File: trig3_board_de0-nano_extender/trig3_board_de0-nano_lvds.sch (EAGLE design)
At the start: 75 parts, among them IC1 SN65LVDT388ADBT, IC2 SN65LVDT388ADBT, J12 4p-2.54, J131 4p-2.54, J14 BU-SMB-V, J19 6HE-160-VG64AC, J3 4p-2.54, J311 4p-2.54, J7 4p-2.54

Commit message: All major components
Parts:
- removed J7: 4p-2.54, Seeed-Connector:DIP-BLACK-FEMALE-HEADER-VERT(4P-2.54)
- added C11, C12, C2, C4, C7, C9: 0.1uF, SparkFun-Capacitors:CAP0805
- added IC3, IC4, IC5, IC6, IC7, IC8: SN65LVDT388ADBT, SamacSys_Parts:SN65LVDT388ADBT
- added J4: 4p-2.54, Seeed-Connector:DIP-BLACK-FEMALE-HEADER-VERT(4P-2.54)
- added JP3, JP4, JP5, JP6, JP7, JP8: 16, pinhead:PINHD-2X8/90
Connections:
- new net N$100: IC6.B2A, JP6.7
- new net N$101: IC6.B2B, JP6.8
- new net N$102: IC6.C1A, JP6.9
- new net N$103: IC6.C1B, JP6.10
- new net N$104: IC6.C2A, JP6.11
- new net N$105: IC6.C2B, JP6.12
- new net N$106: IC6.D1A, JP6.13
- new net N$107: IC6.D1B, JP6.14
- new net N$108: IC6.D2A, JP6.15
- new net N$109: IC6.D2B, JP6.16
- new net N$110: C11.2, IC7.DVCC, IC7.ENA, IC7.ENB, IC7.ENC, IC7.END, IC7.VCC_1, IC7.VCC_2
- new net N$111: C12.2, IC8.DVCC, IC8.ENA, IC8.ENB, IC8.ENC, IC8.END, IC8.VCC_1, IC8.VCC_2
- new net N$112: IC7.A1A, JP7.1
- new net N$113: IC7.A1B, JP7.2
- new net N$114: IC7.A2A, JP7.3
- new net N$115: IC7.A2B, JP7.4
- new net N$116: IC7.B1A, JP7.5
- new net N$117: IC7.B1B, JP7.6
- new net N$118: IC7.B2A, JP7.7
- new net N$119: IC7.B2B, JP7.8
- new net N$120: IC7.C1A, JP7.9
- new net N$121: IC7.C1B, JP7.10
- new net N$122: IC7.C2A, JP7.11
- new net N$123: IC7.C2B, JP7.12
- new net N$124: IC7.D1A, JP7.13
- new net N$125: IC7.D1B, JP7.14
- new net N$126: IC7.D2A, JP7.15
- new net N$127: IC7.D2B, JP7.16
- new net N$128: IC8.A1A, JP8.1
- new net N$129: IC8.A1B, JP8.2
- new net N$130: IC8.A2A, JP8.3
- new net N$131: IC8.A2B, JP8.4
- new net N$132: IC8.B1A, JP8.5
- new net N$133: IC8.B1B, JP8.6
- new net N$134: IC8.B2A, JP8.7
- new net N$135: IC8.B2B, JP8.8
- new net N$136: IC8.C1A, JP8.9
- new net N$137: IC8.C1B, JP8.10
- new net N$138: IC8.C2A, JP8.11
- new net N$139: IC8.C2B, JP8.12
- new net N$140: IC8.D1A, JP8.13
- new net N$141: IC8.D1B, JP8.14
- new net N$142: IC8.D2A, JP8.15
- new net N$143: IC8.D2B, JP8.16
- new net N$42: C2.2, IC3.DVCC, IC3.ENA, IC3.ENB, IC3.ENC, IC3.END, IC3.VCC_1, IC3.VCC_2
- new net N$43: C4.2, IC4.DVCC, IC4.ENA, IC4.ENB, IC4.ENC, IC4.END, IC4.VCC_1, IC4.VCC_2
- new net N$44: IC3.A1A, JP3.1
- new net N$45: IC3.A1B, JP3.2
- new net N$46: IC3.A2A, JP3.3
- new net N$47: IC3.A2B, JP3.4
- new net N$48: IC3.B1A, JP3.5
- new net N$49: IC3.B1B, JP3.6
- new net N$50: IC3.B2A, JP3.7
- new net N$51: IC3.B2B, JP3.8
- new net N$52: IC3.C1A, JP3.9
- new net N$53: IC3.C1B, JP3.10
- new net N$54: IC3.C2A, JP3.11
- new net N$55: IC3.C2B, JP3.12
- new net N$56: IC3.D1A, JP3.13
- new net N$57: IC3.D1B, JP3.14
- new net N$58: IC3.D2A, JP3.15
- new net N$59: IC3.D2B, JP3.16
- new net N$60: IC4.A1A, JP4.1
- new net N$61: IC4.A1B, JP4.2
- new net N$62: IC4.A2A, JP4.3
- new net N$63: IC4.A2B, JP4.4
- new net N$64: IC4.B1A, JP4.5
- new net N$65: IC4.B1B, JP4.6
- new net N$66: IC4.B2A, JP4.7
- new net N$67: IC4.B2B, JP4.8
- new net N$68: IC4.C1A, JP4.9
- new net N$69: IC4.C1B, JP4.10
- new net N$70: IC4.C2A, JP4.11
- new net N$71: IC4.C2B, JP4.12
- new net N$72: IC4.D1A, JP4.13
- new net N$73: IC4.D1B, JP4.14
- new net N$74: IC4.D2A, JP4.15
- new net N$75: IC4.D2B, JP4.16
- new net N$76: C7.2, IC5.DVCC, IC5.ENA, IC5.ENB, IC5.ENC, IC5.END, IC5.VCC_1, IC5.VCC_2
- new net N$77: C9.2, IC6.DVCC, IC6.ENA, IC6.ENB, IC6.ENC, IC6.END, IC6.VCC_1, IC6.VCC_2
- new net N$78: IC5.A1A, JP5.1
- new net N$79: IC5.A1B, JP5.2
- new net N$80: IC5.A2A, JP5.3
- new net N$81: IC5.A2B, JP5.4
- new net N$82: IC5.B1A, JP5.5
- new net N$83: IC5.B1B, JP5.6
- new net N$84: IC5.B2A, JP5.7
- new net N$85: IC5.B2B, JP5.8
- new net N$86: IC5.C1A, JP5.9
- new net N$87: IC5.C1B, JP5.10
- new net N$88: IC5.C2A, JP5.11
- new net N$89: IC5.C2B, JP5.12
- new net N$90: IC5.D1A, JP5.13
- new net N$91: IC5.D1B, JP5.14
- new net N$92: IC5.D2A, JP5.15
- new net N$93: IC5.D2B, JP5.16
- new net N$94: IC6.A1A, JP6.1
- new net N$95: IC6.A1B, JP6.2
- new net N$96: IC6.A2A, JP6.3
- new net N$97: IC6.A2B, JP6.4
- new net N$98: IC6.B1A, JP6.5
- new net N$99: IC6.B1B, JP6.6
- net 5V: now also J3.P$2; no longer J7.P$4
- net GND: now also C11.1, C12.1, C2.1, C4.1, C7.1, C9.1, IC3.AGND_1, IC3.AGND_2, IC3.AGND_3, IC3.DGND_1, IC3.DGND_2, IC3.GND_1, IC3.GND_2, IC4.AGND_1, IC4.AGND_2, IC4.AGND_3, IC4.DGND_1, IC4.DGND_2, IC4.GND_1, IC4.GND_2, IC5.AGND_1, IC5.AGND_2, IC5.AGND_3, IC5.DGND_1, IC5.DGND_2, IC5.GND_1, IC5.GND_2, IC6.AGND_1, IC6.AGND_2, IC6.AGND_3, IC6.DGND_1, IC6.DGND_2, IC6.GND_1, IC6.GND_2, IC7.AGND_1, IC7.AGND_2, IC7.AGND_3, IC7.DGND_1, IC7.DGND_2, IC7.GND_1, IC7.GND_2, IC8.AGND_1, IC8.AGND_2, IC8.AGND_3, IC8.DGND_1, IC8.DGND_2, IC8.GND_1, IC8.GND_2, J3.P$1; no longer J7.P$3
- net GPIO_00_D3: now also IC3.B2Y
- net GPIO_010_B6: now also IC7.C1Y
- net GPIO_011_A6: now also IC7.C2Y
- net GPIO_012_B7: now also IC3.B1Y
- net GPIO_018_E7: now also IC6.D2Y
- net GPIO_019_D8: now also J4.P$3
- net GPIO_01_C3: now also IC4.B2Y
- net GPIO_021_F8: now also IC5.A1Y
- net GPIO_022_F9: now also IC7.B2Y
- net GPIO_023_E9: now also J4.P$2
- net GPIO_024_C9: now also IC4.C2Y
- net GPIO_025_D9: now also IC4.C1Y
- net GPIO_026_E11: now also IC6.C1Y
- net GPIO_028_C11: now also IC7.A2Y
- net GPIO_02_A2: now also IC3.C2Y
- net GPIO_03_A3: now also IC3.C1Y
- net GPIO_0_IN0_A8CLK: now also IC3.D2Y
- net GPIO_0_IN1_B8CLK: now also IC3.D1Y
- net GPIO_10_F13: now also IC6.A2Y; no longer J3.P$2
- net GPIO_110_P11: now also IC6.C2Y
- net GPIO_111_R10: now also IC3.A2Y
- net GPIO_112_N12: now also J4.P$1
- net GPIO_113_P9: now also IC7.D1Y
- net GPIO_115_N11: now also IC7.D2Y
- net GPIO_120_P15: now also IC7.B1Y
- net GPIO_126_L14: now also IC6.B2Y; no longer J7.P$2
- net GPIO_129_L13: now also IC6.B1Y; no longer J7.P$1
- net GPIO_12_T14: now also IC5.C2Y
- net GPIO_132_J13: now also IC7.A1Y
- net GPIO_14_R13: now also IC5.C1Y
- net GPIO_15_T12: now also IC4.D1Y
- net GPIO_16_R12: now also IC4.D2Y
- net GPIO_18_T10: now also IC3.A1Y
- net GPIO_19_R11: now also IC6.A1Y; no longer J3.P$1
- net GPIO_1_IN0_T9CLK: now also IC5.D2Y
- net GPIO_1_IN1_R9CLK: now also IC5.D1Y
- net GPIO_20_A14: now also IC4.A1Y
- net GPIO_210_F14: now also IC8.D2Y
- net GPIO_211_G16: now also IC4.A2Y
- net GPIO_212_G15: now also IC4.B1Y
- net GPIO_21_B16: now also J4.P$4
- net GPIO_22_C14: now also IC8.C2Y
- net GPIO_23_C16: now also IC6.D1Y
- net GPIO_24_C15: now also IC8.C1Y
- net GPIO_25_D16: now also IC8.A1Y
- net GPIO_26_D15: now also IC8.D1Y
- net GPIO_27_D14: now also IC8.A2Y
- net GPIO_28_F15: now also IC8.B1Y
- net GPIO_29_F16: now also IC8.B2Y
- net GPIO_2_IN0_E15CLK: now also IC5.B2Y
- net GPIO_2_IN1_E16CLK: now also IC5.B1Y
- net GPIO_2_IN2_M16CLK: now also IC5.A2Y
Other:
- moved on the sheet: A4, A5, B11, B3, B4, B5, C10, C5, C6, C8, C91, C97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

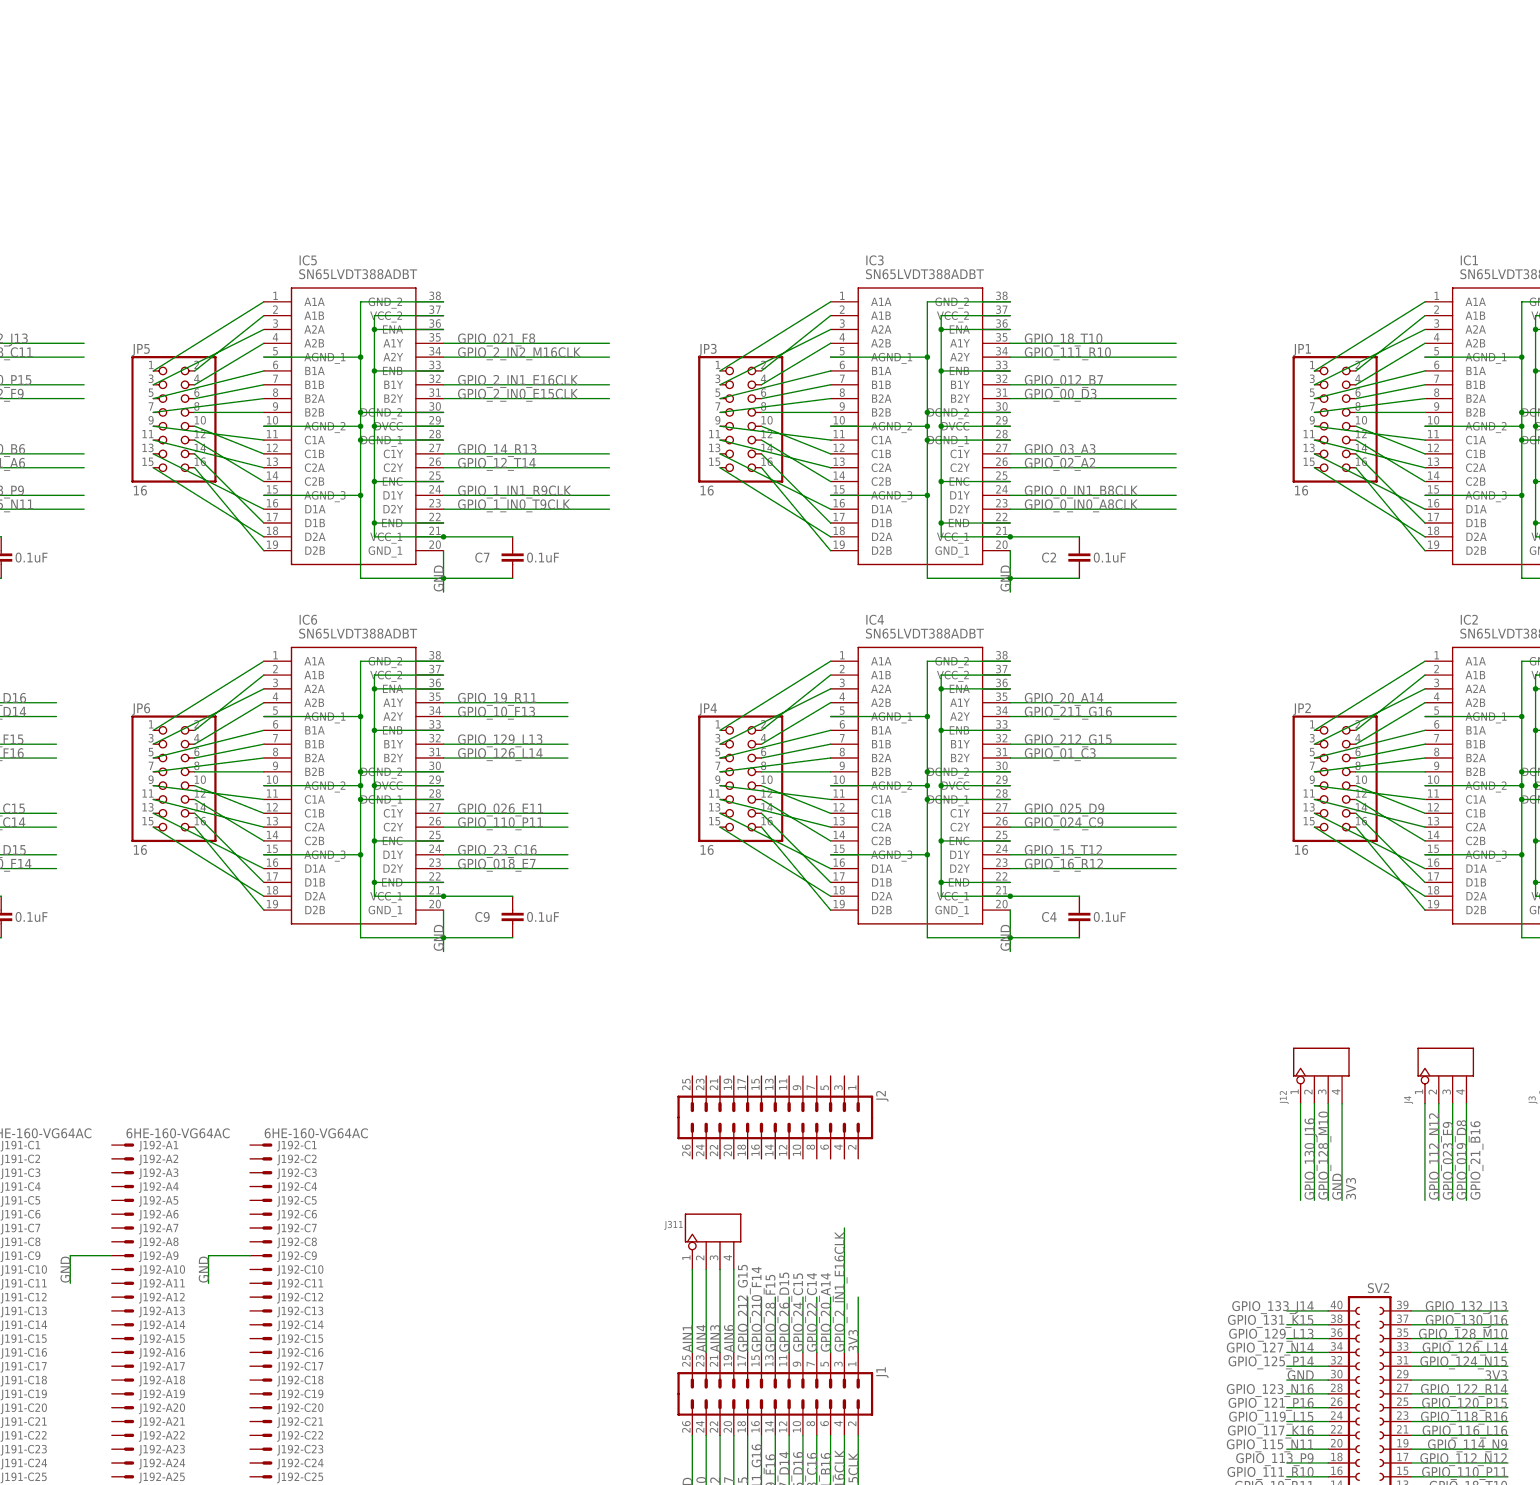
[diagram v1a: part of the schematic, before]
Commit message: Added 3v3 supplies
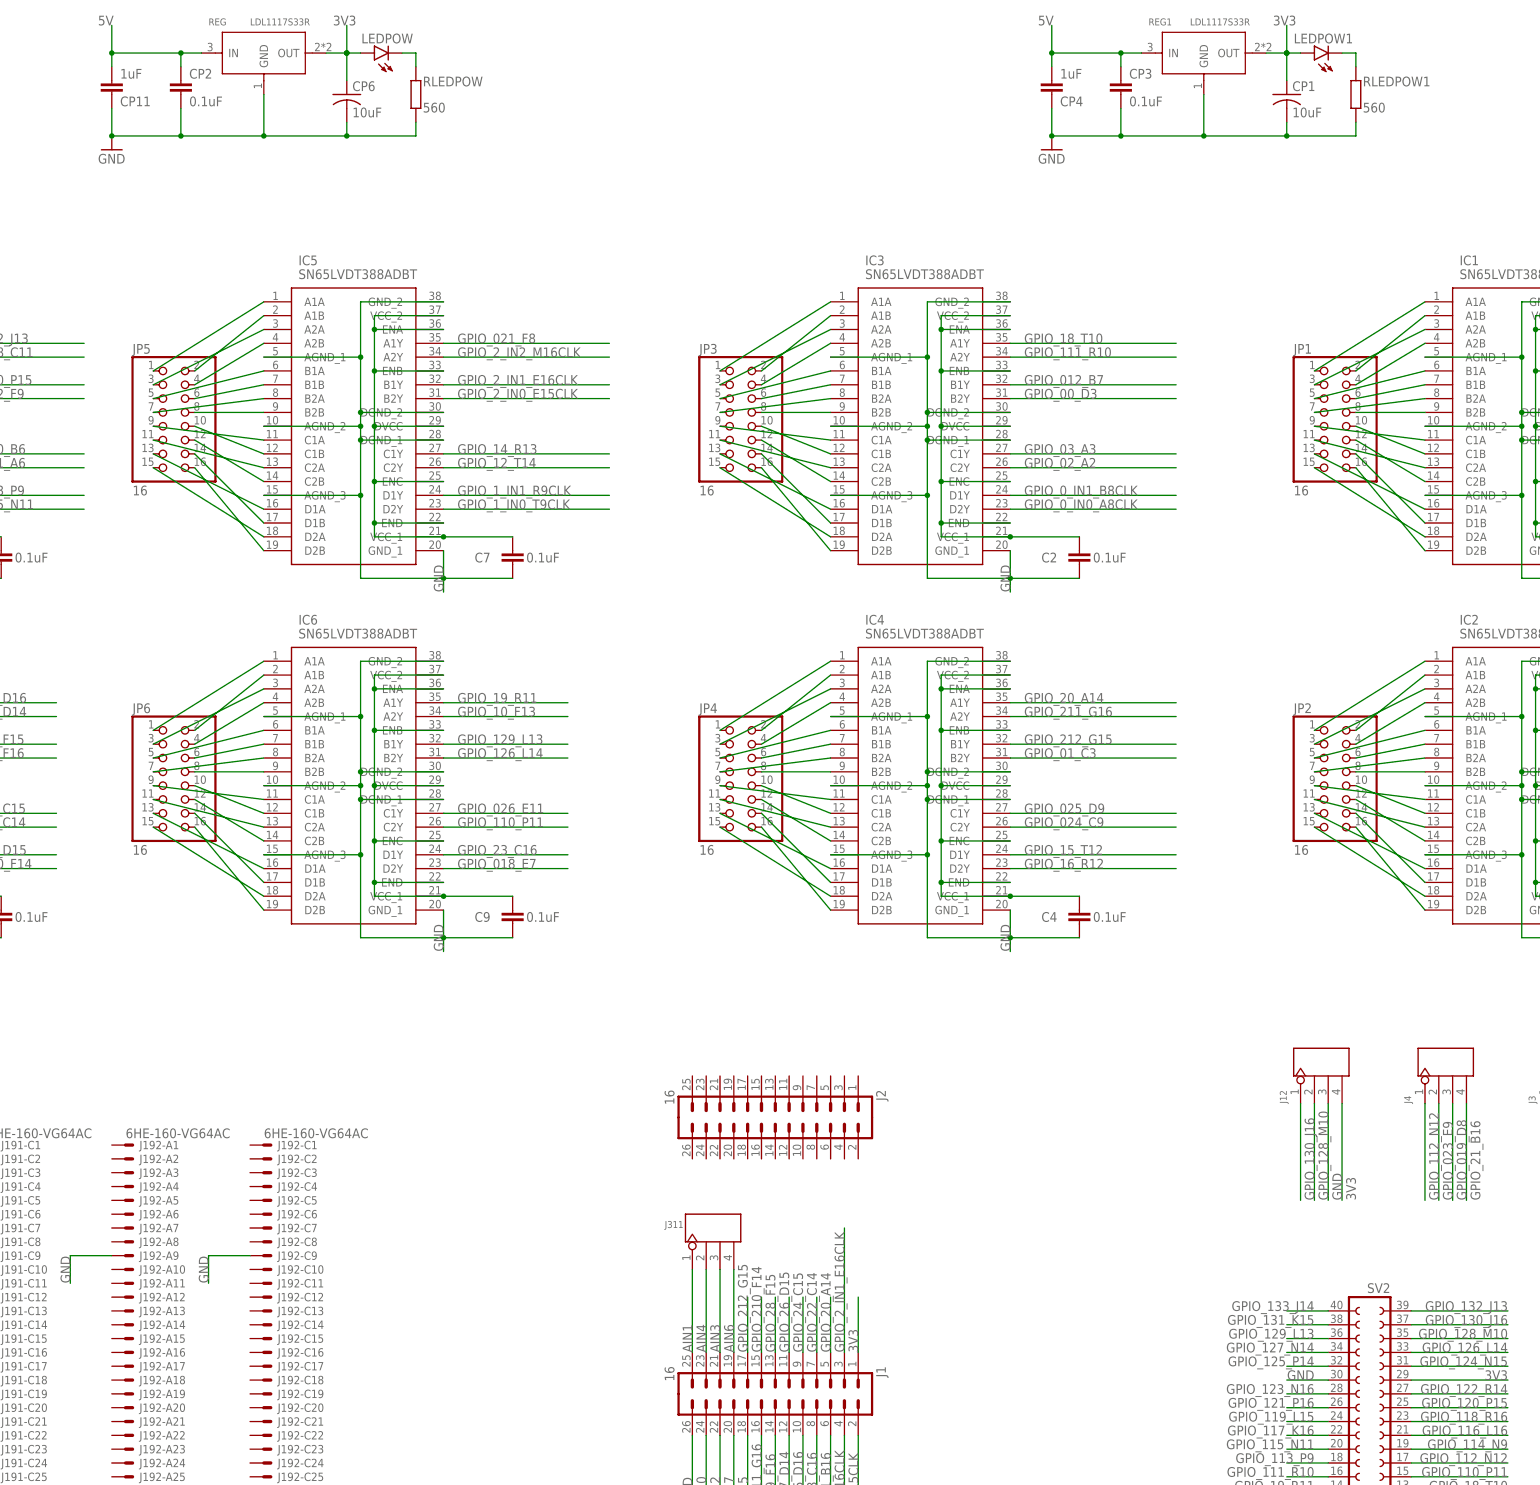
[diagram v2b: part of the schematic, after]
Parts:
- added CP1, CP6: 10uF, rcl@1:C-USC1206
- added CP11, CP4: 1uF, rcl:C-EUC0805K
- added CP2, CP3: 0.1uF, rcl:C-EUC0805K
- added LEDPOW, LEDPOW1: MF-LED-0805-RED, led:LEDSML0805
- added REG, REG1: LDL1117S33R, Seeed-IC-2016:PMIC-CJT1117-3.3(SOT223)
- added RLEDPOW, RLEDPOW1: 560, resistor:R-EU_R0805
- J1, J2: value (none) -> 16
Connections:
- new net N$36: LEDPOW.C, RLEDPOW.1
- new net N$37: LEDPOW1.C, RLEDPOW1.1
- net 3V3: now also CP1.1, CP6.1, LEDPOW.A, LEDPOW1.A, REG.OUT, REG1.OUT
- net 5V: now also CP11.2, CP2.1, CP3.1, CP4.2, REG.IN, REG1.IN
- net GND: now also CP1.2, CP11.1, CP2.2, CP3.2, CP4.1, CP6.2, REG.GND, REG1.GND, RLEDPOW.2, RLEDPOW1.2

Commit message: routed
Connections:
- removed net N$1: C1.2, IC1.DVCC, IC1.ENA, IC1.ENB, IC1.ENC, IC1.END, IC1.VCC_1, IC1.VCC_2
- removed net N$110: C11.2, IC7.DVCC, IC7.ENA, IC7.ENB, IC7.ENC, IC7.END, IC7.VCC_1, IC7.VCC_2
- removed net N$111: C12.2, IC8.DVCC, IC8.ENA, IC8.ENB, IC8.ENC, IC8.END, IC8.VCC_1, IC8.VCC_2
- removed net N$3: C3.2, IC2.DVCC, IC2.ENA, IC2.ENB, IC2.ENC, IC2.END, IC2.VCC_1, IC2.VCC_2
- removed net N$42: C2.2, IC3.DVCC, IC3.ENA, IC3.ENB, IC3.ENC, IC3.END, IC3.VCC_1, IC3.VCC_2
- removed net N$43: C4.2, IC4.DVCC, IC4.ENA, IC4.ENB, IC4.ENC, IC4.END, IC4.VCC_1, IC4.VCC_2
- removed net N$76: C7.2, IC5.DVCC, IC5.ENA, IC5.ENB, IC5.ENC, IC5.END, IC5.VCC_1, IC5.VCC_2
- removed net N$77: C9.2, IC6.DVCC, IC6.ENA, IC6.ENB, IC6.ENC, IC6.END, IC6.VCC_1, IC6.VCC_2
- net 3V3: now also C1.2, C11.2, C12.2, C2.2, C3.2, C4.2, C7.2, C9.2, IC1.DVCC, IC1.ENA, IC1.ENB, IC1.ENC, IC1.END, IC1.VCC_1, IC1.VCC_2, IC2.DVCC, IC2.ENA, IC2.ENB, IC2.ENC, IC2.END, IC2.VCC_1, IC2.VCC_2, IC3.DVCC, IC3.ENA, IC3.ENB, IC3.ENC, IC3.END, IC3.VCC_1, IC3.VCC_2, IC4.DVCC, IC4.ENA, IC4.ENB, IC4.ENC, IC4.END, IC4.VCC_1, IC4.VCC_2, IC5.DVCC, IC5.ENA, IC5.ENB, IC5.ENC, IC5.END, IC5.VCC_1, IC5.VCC_2, IC6.DVCC, IC6.ENA, IC6.ENB, IC6.ENC, IC6.END, IC6.VCC_1, IC6.VCC_2, IC7.DVCC, IC7.ENA, IC7.ENB, IC7.ENC, IC7.END, IC7.VCC_1, IC7.VCC_2, IC8.DVCC, IC8.ENA, IC8.ENB, IC8.ENC, IC8.END, IC8.VCC_1, IC8.VCC_2

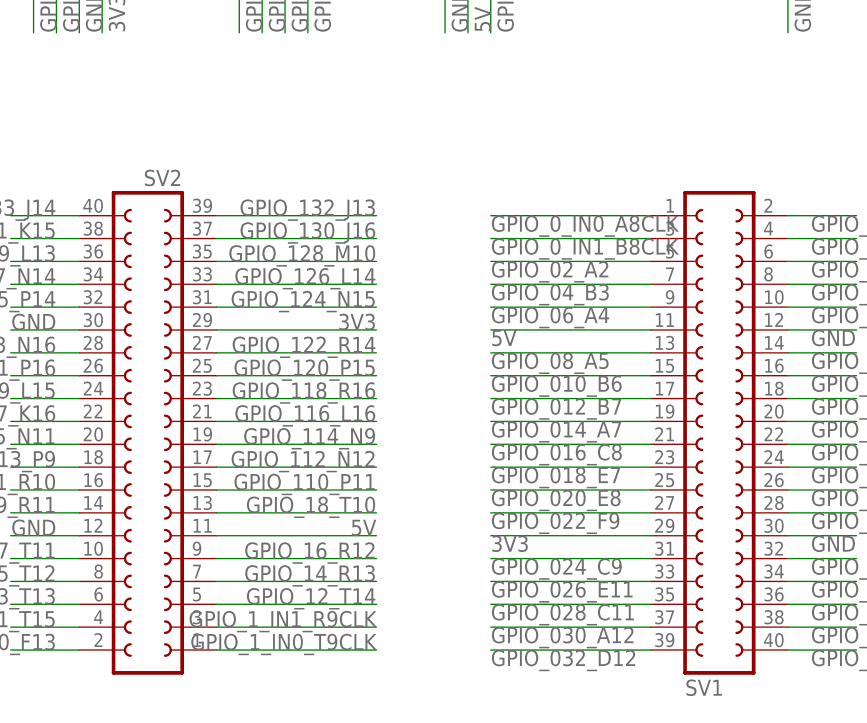
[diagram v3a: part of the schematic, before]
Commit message: routed with gnd on layers 2 and 15
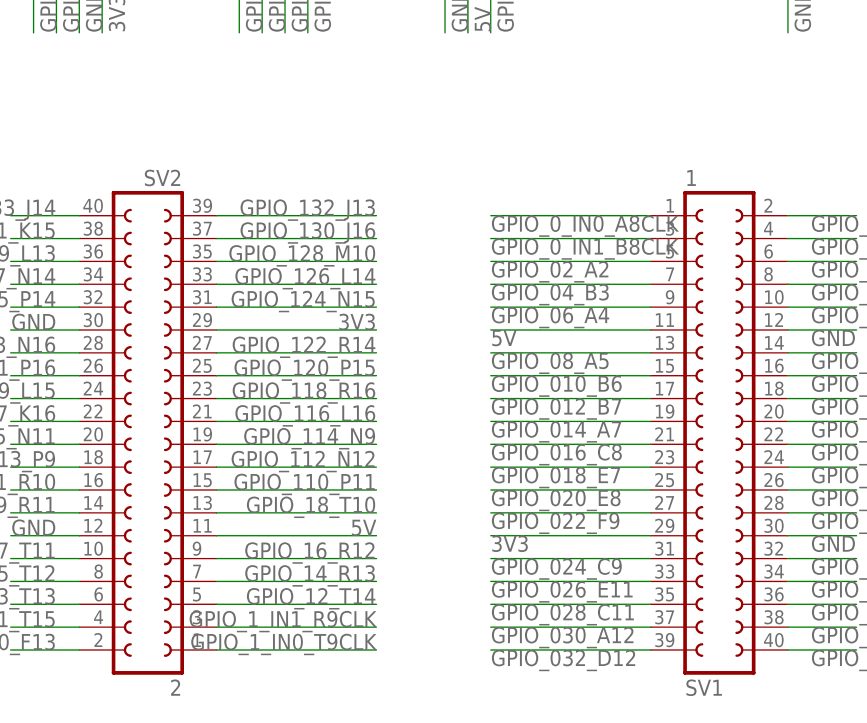
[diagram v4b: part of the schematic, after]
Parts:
- SV1: value (none) -> 1
- SV2: value (none) -> 2
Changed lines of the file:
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@@
 <part name="R17" library="SparkFun-Passives" deviceset="RESISTOR" device="AXIAL-0.3" value="10k"/>
 <part name="J19" library="19inch" library_urn="urn:adsk.eagle:library:79" deviceset="6HE-?-VG64AC" device="160" package3d_urn="urn:adsk.eagle:package:699/1"/>
-<part name="SV1" library="con-lsta" deviceset="FE20-2" device=""/>
-<part name="SV2" library="con-lsta" deviceset="FE20-2" device=""/>
+<part name="SV1" library="con-lsta" deviceset="FE20-2" device="" value="1"/>
+<part name="SV2" library="con-lsta" deviceset="FE20-2" device="" value="2"/>
 <part name="OJ5" library="Seeed-Connector" library_urn="urn:adsk.eagle:library:478" deviceset="DIP-BLACK-MALE-HEADER-VERT(2P-2.54)" device="" package3d_urn="urn:adsk.eagle:package:33132/1" value="2p-2.54"/>
 <part name="OJ6" library="Seeed-Connector" library_urn="urn:adsk.eagle:library:478" deviceset="DIP-BLACK-MALE-HEADER-VERT(2P-2.54)" device="" package3d_urn="urn:adsk.eagle:package:33132/1" value="2p-2.54"/>
@@
 </busses>
 <nets>
-<net name="GND" class="0">
+<net name="GND" class="1">
 <segment>
 <pinref part="VSLUE" gate="G$1" pin="GND"/>
